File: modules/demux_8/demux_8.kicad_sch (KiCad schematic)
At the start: 141 parts, among them J1 Conn_02x18_Row_Letter_First, Q1 2N3904, Q10 2N3904, Q11 2N3904, Q12 2N3904, Q13 2N3904, Q14 2N3904, Q15 2N3904, Q16 2N3904, Q17 2N3904, Q18 2N3904, Q19 2N3904, Q2 2N3906, Q20 2N3904, Q21 2N3904, Q22 2N3904, Q23 2N3904, Q24 2N3904, Q25 2N3904, Q26 2N3904, Q27 2N3904, Q28 2N3904, Q29 2N3904, Q3 2N3906, Q30 2N3904, Q31 2N3904, Q32 2N3904, Q33 2N3904, Q34 2N3904, Q35 2N3904, Q36 2N3904, Q37 2N3904, Q38 2N3904, Q39 2N3904, Q4 2N3906, Q40 2N3904, Q41 2N3904, Q42 2N3904, Q43 2N3904, Q44 2N3904, Q45 2N3904, Q46 2N3904, Q47 2N3904, Q48 2N3904, Q49 2N3904, Q5 2N3904, Q50 2N3904, Q51 2N3904, Q52 2N3904, Q53 2N3904, Q54 2N3904, Q55 2N3904, Q56 2N3904, Q57 2N3904, Q58 2N3904, Q59 2N3904, Q6 2N3904, Q60 2N3904, Q7 2N3904, Q8 2N3904, Q9 2N3904

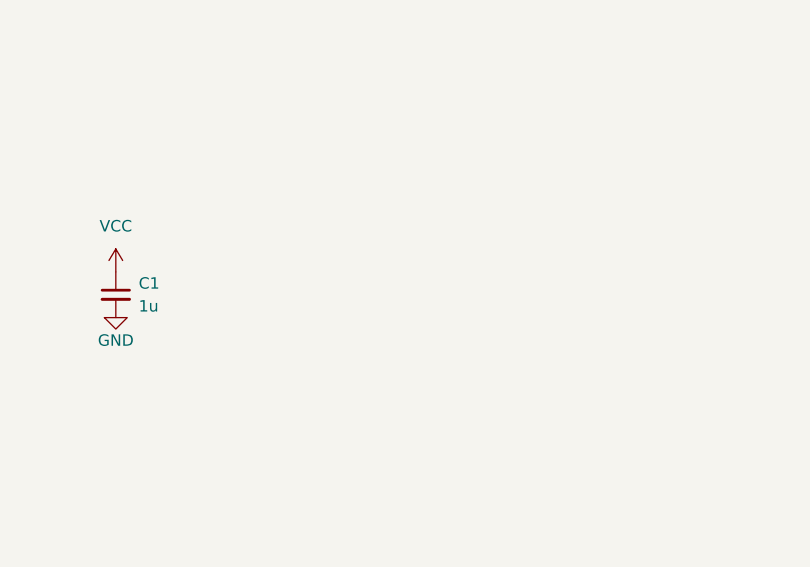
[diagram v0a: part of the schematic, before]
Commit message: More or less finalized PCB for 8-way demux.
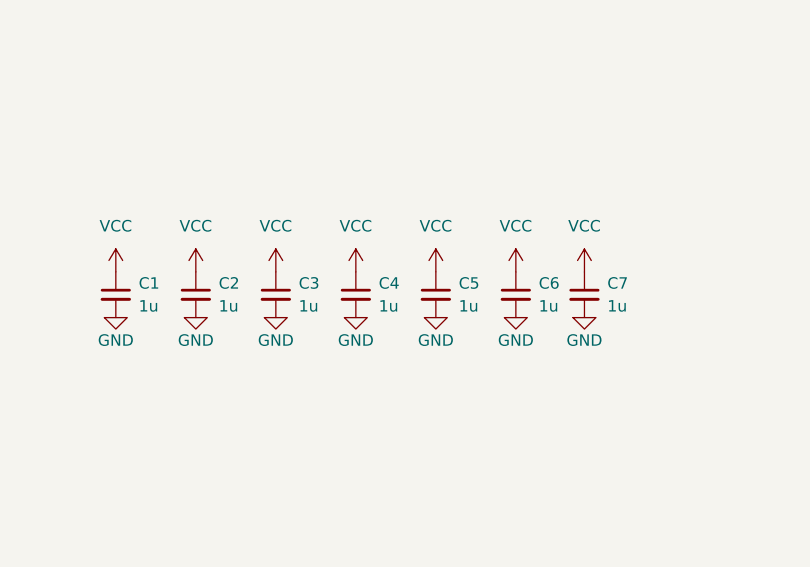
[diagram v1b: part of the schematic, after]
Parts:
- added C2, C3, C4, C5, C6, C7: 1u, Capacitor_SMD:C_0603_1608Metric_Pad1.08x0.95mm_HandSolder, symbol Device:C_Small
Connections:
- net GND: now also C2.2, C3.2, C4.2, C5.2, C6.2, C7.2
- net VCC: now also C2.1, C3.1, C4.1, C5.1, C6.1, C7.1
